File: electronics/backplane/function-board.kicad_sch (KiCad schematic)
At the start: 4 parts, among them X3 MICROMOD_FUNCTION_BOARD_SOCKET

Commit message: Continue backplane PCB
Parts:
- removed TEST1: CLIP_HOOK_PURPLE, Applidyne_Test:KEYSTONE_5119, symbol appli_test_points:CLIP_HOOK_PURPLE
- added TEST2: PROBE_PAD, Applidyne_Test:TP200, symbol appli_test_points:PROBE_PAD
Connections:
- net at X3.40 (EEPROM_WP): now also TEST2.1 (PAD)
- net +POWER: now reaches X3.72 (VCC), X3.74 (VCC)
- no-connect marks 5 -> 6
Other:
- note added: "Control function's onboard regulator"
- note added: "Power is typically 1S LiPo or other regulated 5V source"
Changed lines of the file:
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@@
   (junction (at 105.41 134.62) (diameter 0) (color 0 0 0 0)
   )
+  (junction (at 96.52 96.52) (diameter 0) (color 0 0 0 0)
+  )
   (junction (at 105.41 132.08) (diameter 0) (color 0 0 0 0)
   )
-  (junction (at 105.41 96.52) (diameter 0) (color 0 0 0 0)
-  )
-  (junction (at 105.41 99.06) (diameter 0) (color 0 0 0 0)
-  )
   (junction (at 105.41 127) (diameter 0) (color 0 0 0 0)
   )
@@
   )
   (junction (at 105.41 139.7) (diameter 0) (color 0 0 0 0)
+  )
+  (junction (at 96.52 99.06) (diameter 0) (color 0 0 0 0)
   )
   (junction (at 105.41 129.54) (diameter 0) (color 0 0 0 0)
@@
   (no_connect (at 120.65 114.3))
   (no_connect (at 120.65 119.38))
+  (no_connect (at 120.65 73.66))
   (bus_entry (at 191.135 139.7) (size 2.54 2.54)
     (stroke (width 0) (type default))
@@
     (stroke (width 0) (type default))
   )
-  (wire (pts (xy 105.41 96.52) (xy 120.65 96.52))
+  (wire (pts (xy 96.52 96.52) (xy 120.65 96.52))
     (stroke (width 0) (type default))
   )
@@
     (stroke (width 0) (type default))
   )
+  (wire (pts (xy 95.25 58.42) (xy 95.25 50.8))
+    (stroke (width 0) (type default))
+  )
   (bus (pts (xy 193.675 143.51) (xy 219.71 143.51))
     (stroke (width 0) (type default))
   )
-  (wire (pts (xy 105.41 99.06) (xy 105.41 104.14))
+  (wire (pts (xy 96.52 96.52) (xy 96.52 99.06))
     (stroke (width 0) (type default))
   )
@@
     (stroke (width 0) (type default))
   )
-  (wire (pts (xy 105.41 93.98) (xy 120.65 93.98))
-    (stroke (width 0) (type default))
-  )
   (bus (pts (xy 193.675 134.62) (xy 193.675 137.16))
     (stroke (width 0) (type default))
@@
     (stroke (width 0) (type default))
   )
-  (wire (pts (xy 105.41 99.06) (xy 120.65 99.06))
+  (wire (pts (xy 96.52 99.06) (xy 120.65 99.06))
     (stroke (width 0) (type default))
   )
@@
     (stroke (width 0) (type default))
   )
-  (wire (pts (xy 105.41 99.06) (xy 105.41 96.52))
-    (stroke (width 0) (type default))
-  )
   (wire (pts (xy 179.07 58.42) (xy 198.12 58.42))
     (stroke (width 0) (type default))
@@
     (stroke (width 0) (type default))
   )
+  (wire (pts (xy 96.52 93.98) (xy 96.52 96.52))
+    (stroke (width 0) (type default))
+  )
   (wire (pts (xy 179.07 134.62) (xy 191.135 134.62))
     (stroke (width 0) (type default))
@@
     (stroke (width 0) (type default))
   )
-  (wire (pts (xy 92.71 50.8) (xy 92.71 58.42))
+  (wire (pts (xy 96.52 99.06) (xy 96.52 102.87))
     (stroke (width 0) (type default))
   )
@@
     (stroke (width 0) (type default))
   )
-  (wire (pts (xy 118.11 58.42) (xy 92.71 58.42))
+  (wire (pts (xy 118.11 58.42) (xy 95.25 58.42))
     (stroke (width 0) (type default))
   )
@@
     (stroke (width 0) (type default))
   )
-  (wire (pts (xy 105.41 93.98) (xy 105.41 96.52))
-    (stroke (width 0) (type default))
-  )
   (bus (pts (xy 200.66 55.88) (xy 200.66 58.42))
     (stroke (width 0) (type default))
@@
     (stroke (width 0) (type default))
   )
+  (wire (pts (xy 96.52 93.98) (xy 120.65 93.98))
+    (stroke (width 0) (type default))
+  )
   (wire (pts (xy 118.11 60.96) (xy 118.11 58.42))
     (stroke (width 0) (type default))
@@
     (effects (font (size 1.27 1.27)) (justify left bottom))
   )
-  (text "Set function board ID\nEEPROM addr to default" (at 102.87 99.06 0)
+  (text "Set function board ID\nEEPROM addr to default" (at 93.98 97.79 0)
     (effects (font (size 1.27 1.27)) (justify right bottom))
+  )
+  (text "Control function's onboard regulator" (at 64.77 67.31 0)
+    (effects (font (size 1.27 1.27)) (justify left bottom))
+  )
+  (text "Power is typically 1S LiPo\nor other regulated 5V source"
+    (at 64.77 57.15 0)
+    (effects (font (size 1.27 1.27)) (justify left bottom))
   )
   (label "TX" (at 185.42 93.98 0) (fields_autoplaced)
@@
     )
   )
-  (symbol (lib_id "appli_power:GND") (at 105.41 104.14 0) (unit 1)
+  (symbol (lib_id "appli_power:GND") (at 96.52 102.87 0) (unit 1)
     (in_bom yes) (on_board yes) (dnp no) (fields_autoplaced)
-    (property "Reference" "#PWR021" (at 105.41 110.49 0)
-      (effects (font (size 1.27 1.27)) hide)
-    )
-    (property "Value" "GND" (at 105.41 109.22 0)
+    (property "Reference" "#PWR021" (at 96.52 109.22 0)
+      (effects (font (size 1.27 1.27)) hide)
+    )
+    (property "Value" "GND" (at 96.52 107.95 0)
       (effects (font (size 1.27 1.27)))
     )
-    (property "Footprint" "" (at 105.41 104.14 0)
-      (effects (font (size 1.27 1.27)) hide)
-    )
-    (property "Datasheet" "" (at 105.41 104.14 0)
+    (property "Footprint" "" (at 96.52 102.87 0)
+      (effects (font (size 1.27 1.27)) hide)
+    )
+    (property "Datasheet" "" (at 96.52 102.87 0)
       (effects (font (size 1.27 1.27)) hide)
     )
@@
     )
   )
-  (symbol (lib_id "appli_test_points:CLIP_HOOK_PURPLE") (at 118.11 101.6 0) (mirror x) (unit 1)
+  (symbol (lib_id "appli_power:+POWER") (at 95.25 50.8 0) (unit 1)
     (in_bom yes) (on_board yes) (dnp no) (fields_autoplaced)
-    (property "Reference" "TEST1" (at 113.03 103.5049 0)
-      (effects (font (size 0.9906 0.9906)) (justify right))
-    )
-    (property "Value" "CLIP_HOOK_PURPLE" (at 119.38 101.6 0)
-      (effects (font (size 0.9906 0.9906)) (justify left top) hide)
-    )
-    (property "Footprint" "Applidyne_Test:KEYSTONE_5119" (at 119.38 100.33 0)
-      (effects (font (size 0.9906 0.9906)) (justify left top) hide)
-    )
-    (property "Datasheet" "http://www.farnell.com/datasheets/1703983.pdf" (at 119.38 96.52 0)
-      (effects (font (size 0.9906 0.9906)) (justify left bottom) hide)
-    )
-    (property "manf" "KEYSTONE" (at 119.38 99.06 0)
-      (effects (font (size 0.9906 0.9906)) (justify left top) hide)
-    )
-    (property "manf#" "5119" (at 119.38 95.25 0)
-      (effects (font (size 0.9906 0.9906)) (justify left bottom) hide)
-    )
-    (property "Supplier" "Element14" (at 119.38 93.98 0)
-      (effects (font (size 0.9906 0.9906)) (justify left bottom) hide)
-    )
-    (property "Supplier Part No" "2501305" (at 119.38 92.71 0)
-      (effects (font (size 0.9906 0.9906)) (justify left bottom) hide)
-    )
-    (property "Supplier URL" "http://au.element14.com/keystone/5119/test-point-pcb-purple-through/dp/2501305" (at 119.38 91.44 0)
-      (effects (font (size 0.9906 0.9906)) (justify left bottom) hide)
-    )
-    (property "Supplier Price" "0.3" (at 119.38 90.17 0)
-      (effects (font (size 0.9906 0.9906)) (justify left bottom) hide)
-    )
-    (property "Suppier Price Break" "1" (at 119.38 88.9 0)
-      (effects (font (size 0.9906 0.9906)) (justify left bottom) hide)
+    (property "Reference" "#PWR046" (at 95.25 52.07 0)
+      (effects (font (size 0.508 0.508)) hide)
+    )
+    (property "Value" "+POWER" (at 95.25 46.99 0)
+      (effects (font (size 0.762 0.762)))
+    )
+    (property "Footprint" "" (at 95.25 50.8 0)
+      (effects (font (size 1.524 1.524)))
+    )
+    (property "Datasheet" "" (at 95.25 50.8 0)
+      (effects (font (size 1.524 1.524)))
     )
     (pin "1")
     (instances
       (project "backplane"
-        (path "/0bfdf1e4-b99d-46d4-adfc-42d352d37946"
-          (reference "TEST1") (unit 1)
-        )
         (path "/0bfdf1e4-b99d-46d4-adfc-42d352d37946/53f921ee-8079-43f9-aa5b-2041db09aea1"
-          (reference "TEST1") (unit 1)
+          (reference "#PWR046") (unit 1)
         )
       )
+    )
+  )
+  (symbol (lib_id "appli_test_points:PROBE_PAD") (at 118.11 101.6 0) (mirror x) (unit 1)
+    (in_bom yes) (on_board yes) (dnp no) (fields_autoplaced)
+    (property "Reference" "TEST2" (at 118.11 99.06 0)
+      (effects (font (size 1.524 1.524)) hide)
+    )
+    (property "Value" "PROBE_PAD" (at 113.03 102.235 0)
+      (effects (font (size 1.524 1.524)) (justify right))
+    )
+    (property "Footprint" "Applidyne_Test:TP200" (at 113.03 103.505 0)
+      (effects (font (size 1.524 1.524)) (justify right) hide)
+    )
+    (property "Datasheet" "" (at 118.11 99.06 0)
+      (effects (font (size 1.524 1.524)))
+    )
+    (property "manf" "N/A" (at 118.11 87.63 0)
+      (effects (font (size 1.524 1.524)) hide)
+    )
+    (property "manf#" "N/A" (at 118.11 85.09 0)
+      (effects (font (size 1.524 1.524)) hide)
+    )
+    (property "Supplier" "N/A" (at 118.11 82.55 0)
+      (effects (font (size 1.524 1.524)) hide)
+    )
+    (property "Supplier URL" "#" (at 118.11 80.01 0)
+      (effects (font (size 1.524 1.524)) hide)
+    )
+    (property "Supplier Price" "0" (at 118.11 90.17 0)
+      (effects (font (size 1.524 1.524)) hide)
+    )
+    (property "Supplier Price Break" "0" (at 118.11 92.71 0)
+      (effects (font (size 1.524 1.524)) hide)
+    )
+    (property "Installed" "DNP" (at 113.03 104.775 0)
+      (effects (font (size 1.524 1.524)) (justify right))
+    )
+    (pin "1")
+    (instances
+      (project "backplane"
+        (path "/0bfdf1e4-b99d-46d4-adfc-42d352d37946/53f921ee-8079-43f9-aa5b-2041db09aea1"
+          (reference "TEST2") (unit 1)
+        )
+      )

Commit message: Continue backplane
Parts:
- added R14: 0R_QUAD_ARRAY_1608M, Applidyne_Resistor:R_Array_Concave_4x1608M, symbol appli_resistor:0R_QUAD_ARRAY_1608M
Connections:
- net CTS: now also R14.5; no longer X3.16 (FUNC_RTS)
- net RTS: now also R14.6; no longer X3.18 (FUNC_CTS)
- net RX: now also R14.7; no longer X3.13 (FUNC_TX)
- net TX: now also R14.8; no longer X3.15 (FUNC_RX)
- new net: R14.3, X3.18 (FUNC_CTS)
- new net: R14.2, X3.13 (FUNC_TX)
- new net: R14.1, X3.15 (FUNC_RX)
- new net: R14.4, X3.16 (FUNC_RTS)
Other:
- note added: "Quad resistor allows serial lines to be 'cut' from a function board that doesn't use them"

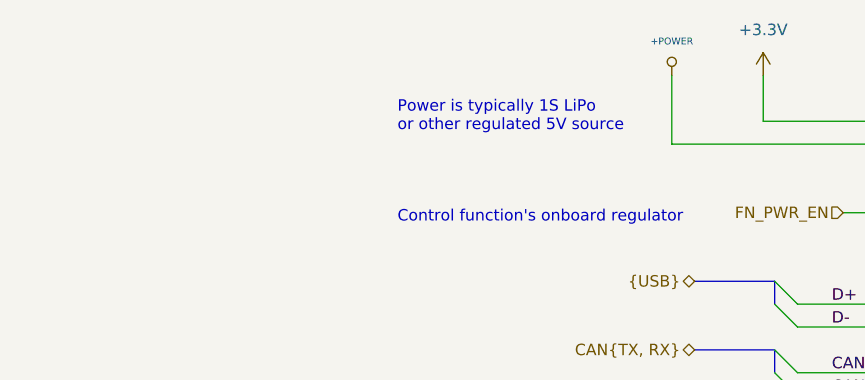
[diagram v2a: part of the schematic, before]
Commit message: Continue schematic tweaks, start routing backplane
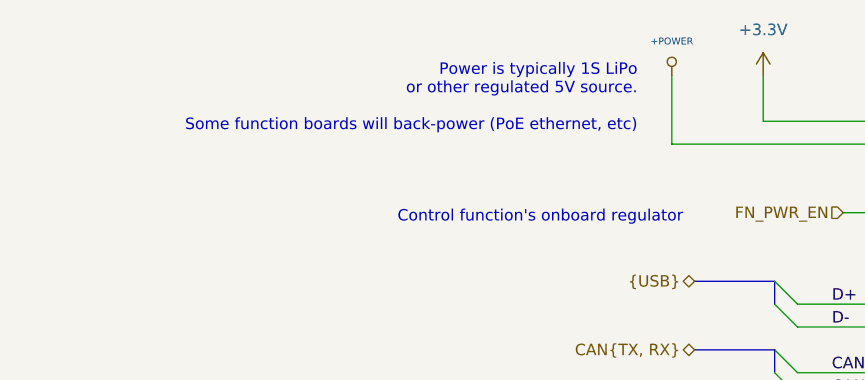
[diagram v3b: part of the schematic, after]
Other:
- note added: "Power is typically 1S LiPo or other regulated 5V source. Some function boards will back-power (PoE ethernet, etc)"
- note removed: "Power is typically 1S LiPo or other regulated 5V source"
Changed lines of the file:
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@@
     (effects (font (size 1.27 1.27)) (justify left bottom))
   )
-  (text "Power is typically 1S LiPo\nor other regulated 5V source"
-    (at 64.77 57.15 0)
-    (effects (font (size 1.27 1.27)) (justify left bottom))
+  (text "Power is typically 1S LiPo\nor other regulated 5V source.\n\nSome function boards will back-power (PoE ethernet, etc)"
+    (at 91.44 57.15 0)
+    (effects (font (size 1.27 1.27)) (justify right bottom))
   )
   (label "TX" (at 203.835 93.98 0) (fields_autoplaced)
